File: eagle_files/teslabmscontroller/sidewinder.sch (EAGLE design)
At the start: 41 parts, among them J1 TERMINAL12, J2 TERMINAL12, Q1 2N3704, Q2 2N3906, T1 V_REG_317SINK, U1 G3VM41, U2 G3VM41, U3 G3VM41, U4 SN65HVD230, U5 SP720APP, U6 SP720APP

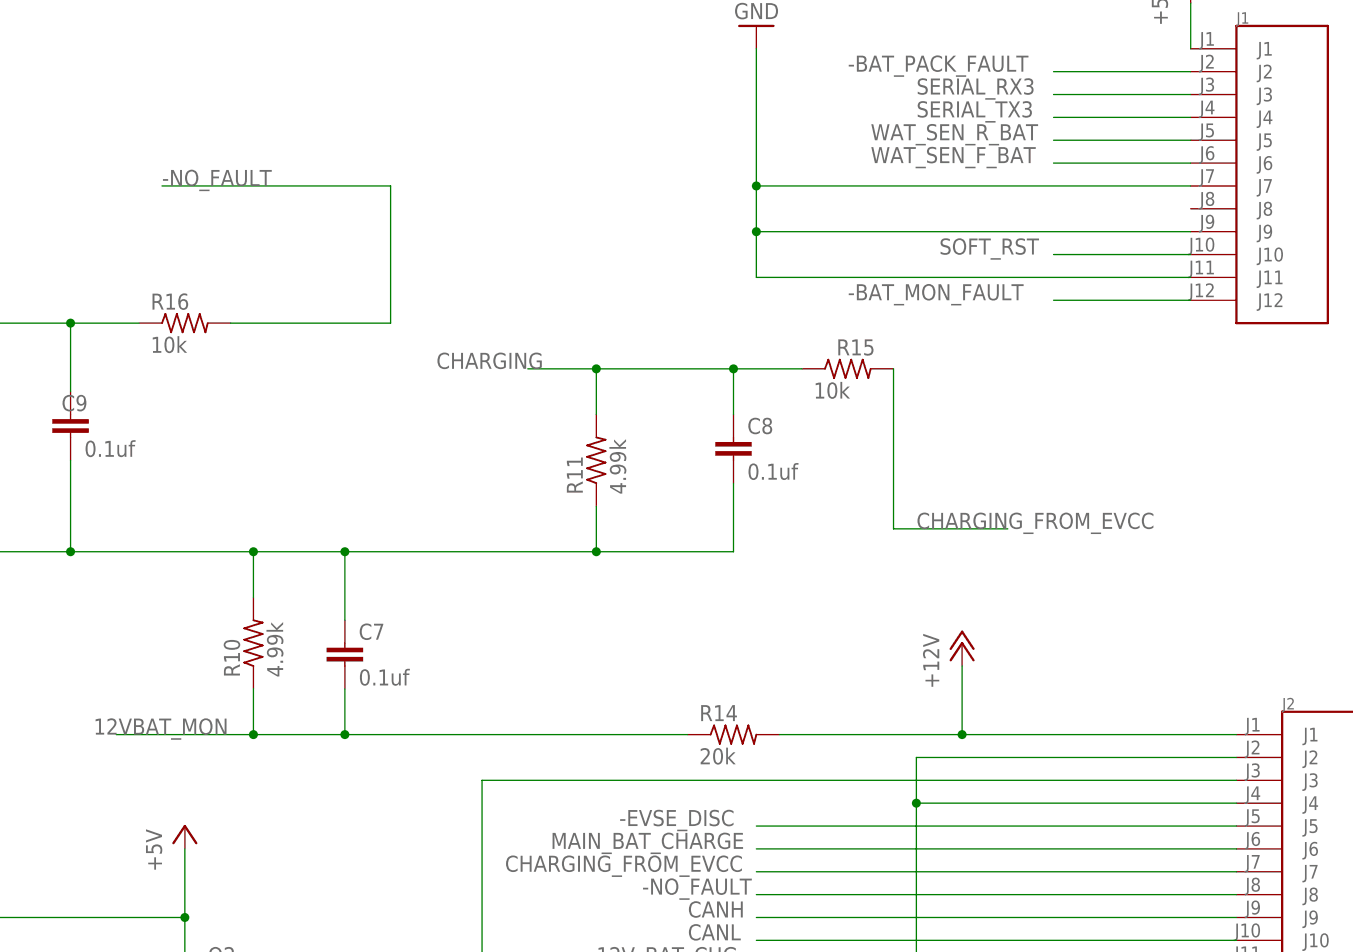
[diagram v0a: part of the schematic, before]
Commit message: fixed RUN
RUN signal was absent from connector
flipped whole board so silk alligns with OLED
fixed routing issu of can chip
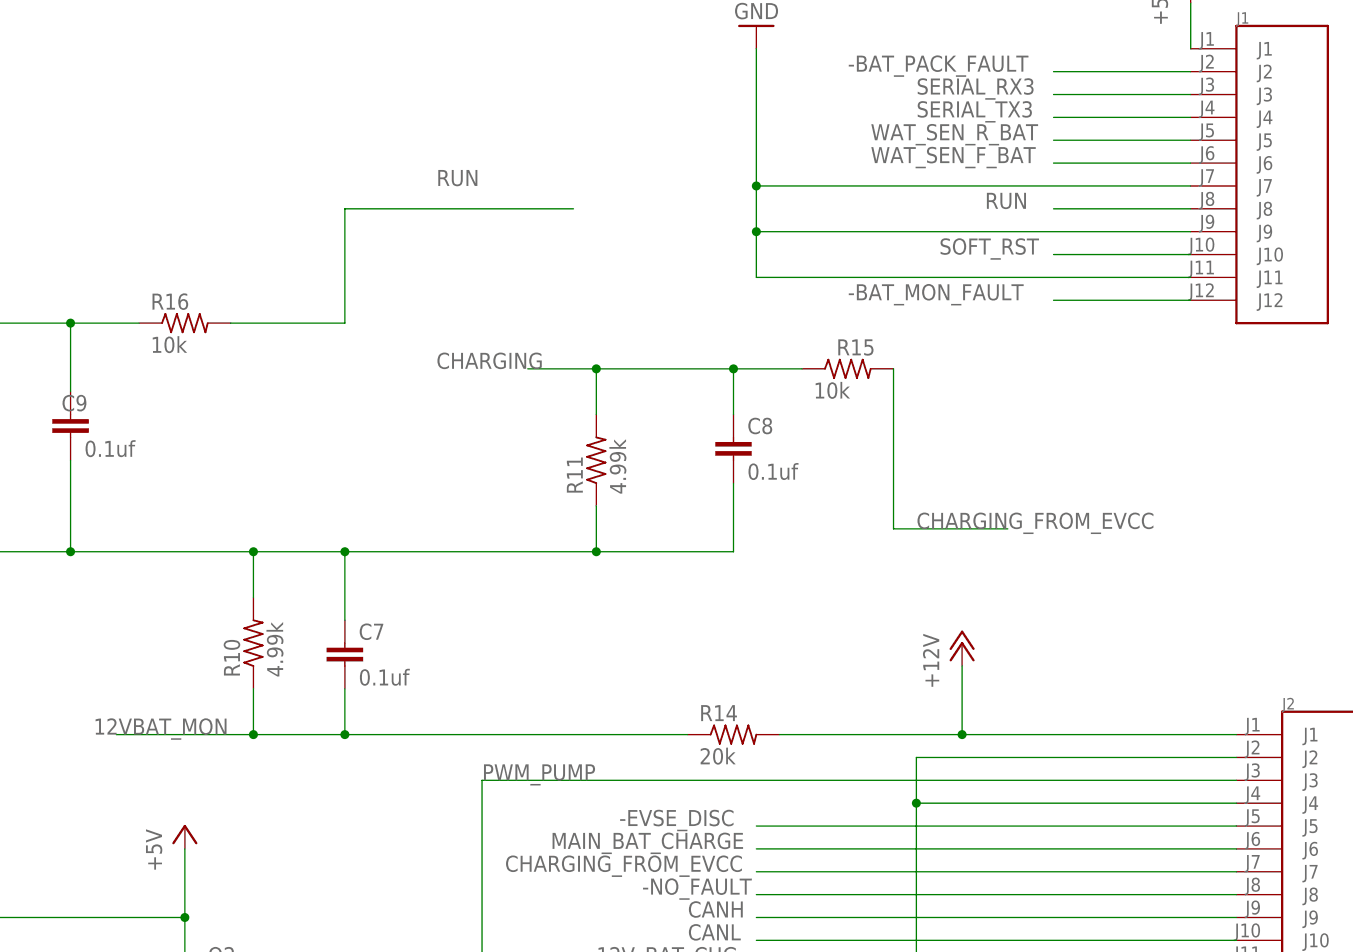
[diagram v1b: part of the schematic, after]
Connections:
- net N$4 renamed PWM_PUMP
- new net RUN: J1.J8, R16.2
- net -NO_FAULT: no longer R16.2
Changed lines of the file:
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@@
 <clearance class="0" value="0.3048"/>
 </class>
-<class number="1" name="VCC" width="0.6096" drill="0.508">
-<clearance class="1" value="0.6096"/>
+<class number="1" name="VCC" width="0.508" drill="0.508">
+<clearance class="1" value="0.508"/>
 </class>
 </classes>
@@
 <wire x1="73.66" y1="-83.82" x2="116.84" y2="-83.82" width="0.1524" layer="91"/>
 </segment>
-<segment>
-<pinref part="R16" gate="G$1" pin="2"/>
-<wire x1="167.64" y1="96.52" x2="149.86" y2="96.52" width="0.1524" layer="91"/>
-<wire x1="142.24" y1="111.76" x2="167.64" y2="111.76" width="0.1524" layer="91"/>
-<wire x1="167.64" y1="111.76" x2="167.64" y2="96.52" width="0.1524" layer="91"/>
-<label x="142.24" y="111.76" size="1.778" layer="95"/>
-</segment>
 </net>
 <net name="N$1" class="0">
@@
 </segment>
 </net>
-<net name="N$4" class="0">
+<net name="PWM_PUMP" class="0">
 <segment>
 <pinref part="R5" gate="G$1" pin="2"/>
@@
 <wire x1="165.1" y1="12.7" x2="165.1" y2="15.24" width="0.1524" layer="91"/>
 <junction x="165.1" y="15.24"/>
+<label x="177.8" y="45.72" size="1.778" layer="95"/>
 </segment>
 </net>
@@
 </segment>
 </net>
+<net name="RUN" class="0">
+<segment>
+<pinref part="R16" gate="G$1" pin="2"/>
+<wire x1="149.86" y1="96.52" x2="162.56" y2="96.52" width="0.1524" layer="91"/>
+<wire x1="162.56" y1="96.52" x2="162.56" y2="109.22" width="0.1524" layer="91"/>
+<wire x1="162.56" y1="109.22" x2="187.96" y2="109.22" width="0.1524" layer="91"/>
+<label x="172.72" y="111.76" size="1.778" layer="95"/>
+</segment>
+<segment>
+<pinref part="J1" gate="G$1" pin="J8"/>
+<wire x1="256.54" y1="109.22" x2="241.3" y2="109.22" width="0.1524" layer="91"/>
+<label x="233.68" y="109.22" size="1.778" layer="95"/>
+</segment>
+</net>
